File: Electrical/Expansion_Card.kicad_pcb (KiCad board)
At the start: 2 copper layers, 26 x 30 mm, 15 parts, among them J1 SJ-3501-SMT-TR, J2 SJ-3501-SMT-TR, P1 USB_C_Plug_USB2.0, U1 AP2112K-3.3, U2 PCM2906, U3 TPA6132A2RTE

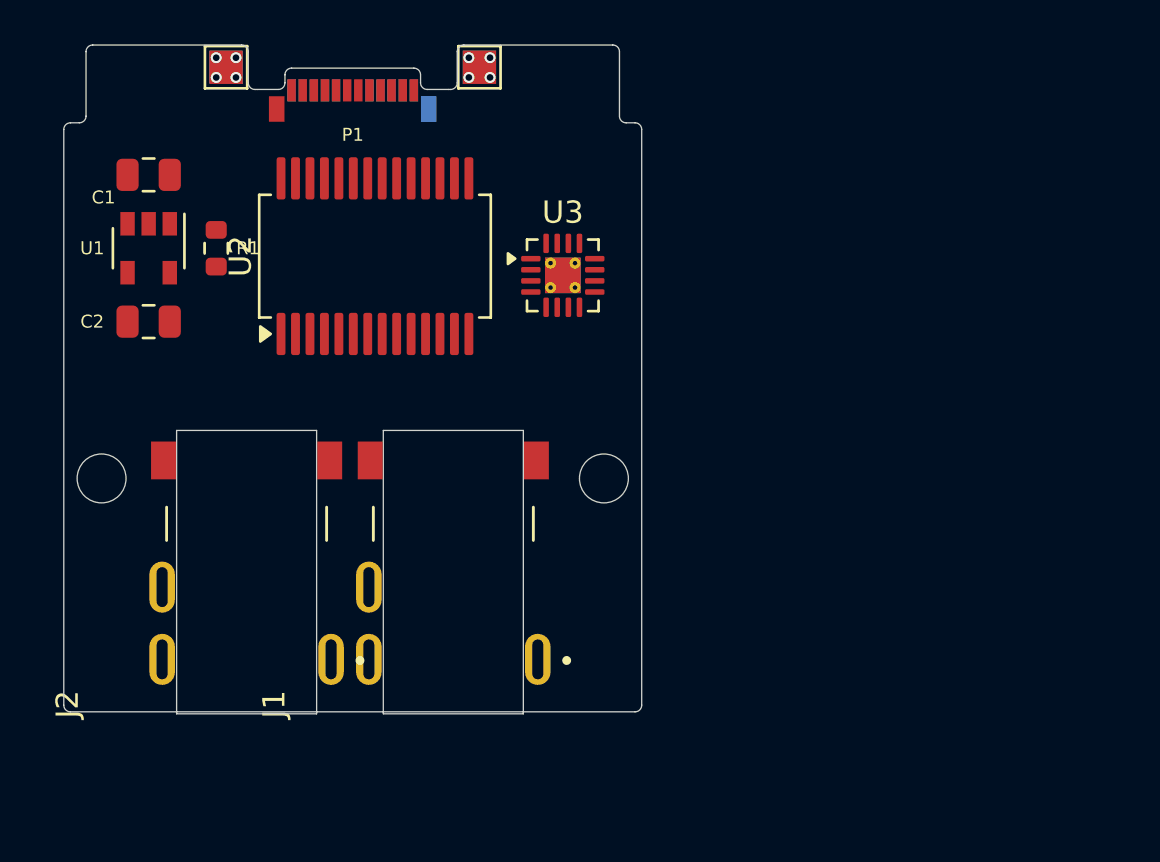
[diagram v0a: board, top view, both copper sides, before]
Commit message: New footprints and components added
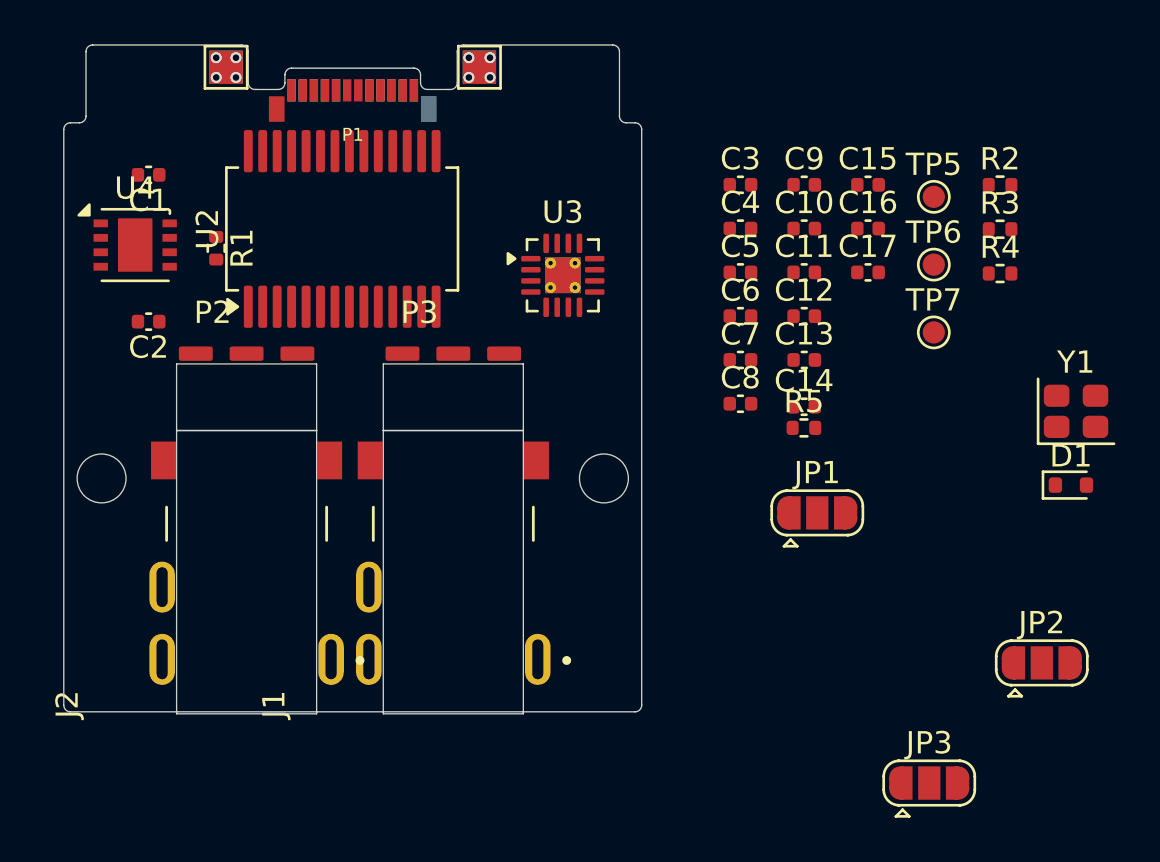
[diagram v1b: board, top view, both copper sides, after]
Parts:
- removed U1: AP2112K-3.3, Package_TO_SOT_SMD:SOT-23-5
- added C10: 1uF, Capacitor_SMD:C_0402_1005Metric, F.Cu at (160.3, 135.3)
- added C11: 1uF, Capacitor_SMD:C_0402_1005Metric, F.Cu at (160.3, 137.2)
- added C12: 1uF, Capacitor_SMD:C_0402_1005Metric, F.Cu at (160.3, 139.2)
- added C13: 1uF, Capacitor_SMD:C_0402_1005Metric, F.Cu at (160.3, 141.2)
- added C14: 1uF, Capacitor_SMD:C_0402_1005Metric, F.Cu at (160.3, 143.3)
- added C15: 1uF, Capacitor_SMD:C_0402_1005Metric, F.Cu at (163.2, 133.3)
- added C16: 2.2uF, Capacitor_SMD:C_0402_1005Metric, F.Cu at (163.2, 135.3)
- added C17: 2.2uF, Capacitor_SMD:C_0402_1005Metric, F.Cu at (163.2, 137.2)
- added C3: 8pF, Capacitor_SMD:C_0402_1005Metric, F.Cu at (157.4, 133.3)
- added C4: 8pF, Capacitor_SMD:C_0402_1005Metric, F.Cu at (157.4, 135.3)
- added C5: 10uF, Capacitor_SMD:C_0402_1005Metric, F.Cu at (157.4, 137.2)
- added C6: 10uF, Capacitor_SMD:C_0402_1005Metric, F.Cu at (157.4, 139.2)
- added C7: 1uF, Capacitor_SMD:C_0402_1005Metric, F.Cu at (157.4, 141.2)
- added C8: 1uF, Capacitor_SMD:C_0402_1005Metric, F.Cu at (157.4, 143.1)
- added C9: 1uF, Capacitor_SMD:C_0402_1005Metric, F.Cu at (160.3, 133.3)
- added D1: CDBU0130-HF, Diode_SMD:D_SOD-523, F.Cu at (172.3, 146.8)
- added JP1: SolderJumper_3_Open, Jumper:SolderJumper-3_P1.3mm_Open_RoundedPad1.0x1.5mm, F.Cu at (160.9, 148.1)
- added JP2: SolderJumper_3_Open, Jumper:SolderJumper-3_P1.3mm_Open_RoundedPad1.0x1.5mm, F.Cu at (171.0, 154.8)
- added JP3: SolderJumper_3_Open, Jumper:SolderJumper-3_P1.3mm_Open_RoundedPad1.0x1.5mm, F.Cu at (165.9, 160.2)
- added P2: ~, Expansion_Card:TX_RX_module, F.Cu at (135.2, 142.8)
- added P3: ~, Expansion_Card:TX_RX_module, F.Cu at (144.5, 142.8)
- added R2: 1.5k, Resistor_SMD:R_0402_1005Metric, F.Cu at (169.1, 133.3)
- added R3: 22, Resistor_SMD:R_0402_1005Metric, F.Cu at (169.1, 135.3)
- added R4: 22, Resistor_SMD:R_0402_1005Metric, F.Cu at (169.1, 137.3)
- added R5: 1M, Resistor_SMD:R_0402_1005Metric, F.Cu at (160.3, 144.2)
- added TP5: TestPoint, TestPoint:TestPoint_Pad_D1.0mm, F.Cu at (166.1, 133.8)
- added TP6: TestPoint, TestPoint:TestPoint_Pad_D1.0mm, F.Cu at (166.1, 136.9)
- added TP7: TestPoint, TestPoint:TestPoint_Pad_D1.0mm, F.Cu at (166.1, 139.9)
- added U4: LDLN050PUR, Package_DFN_QFN:DFN-8-1EP_3x3mm_P0.65mm_EP1.55x2.4mm, F.Cu at (130.2, 136.0)
- added Y1: 120-8-36B-CWY-TR, Crystal:Crystal_SMD_2520-4Pin_2.5x2.0mm, F.Cu at (172.5, 143.5)
- C1, C2: footprint Capacitor_SMD:C_0805_2012Metric -> Capacitor_SMD:C_0402_1005Metric
- R1: footprint Resistor_SMD:R_0603_1608Metric -> Resistor_SMD:R_0402_1005Metric
- moved U2 1.92 mm to (139.5, 135.3)
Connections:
- C2 pad 1: +3.3V -> VCC
- J1 pad 1: unconnected-(J1-Pad1) -> GND
- J1 pad 2: unconnected-(J1-Pad2) -> Net-(U3-OUTL)
- J1 pad 3: unconnected-(J1-Pad3) -> Net-(U3-OUTR)
- U2 pad 1: unconnected-(U2-D+-Pad1) -> Net-(U2-D+)
- U2 pad 10: unconnected-(U2-VCCCI-Pad10) -> VCCI
- U2 pad 11: unconnected-(U2-AGNDC-Pad11) -> GND
- U2 pad 14: unconnected-(U2-VCOM-Pad14) -> Net-(U2-VCOM)
- U2 pad 15: unconnected-(U2-VOUTR-Pad15) -> Net-(U2-VOUTR)
- U2 pad 16: unconnected-(U2-VOUTL-Pad16) -> Net-(U2-VOUTL)
- U2 pad 17: unconnected-(U2-VCCP1I-Pad17) -> Net-(U2-VCCP1I)
- U2 pad 18: unconnected-(U2-AGNDP-Pad18) -> GND
- U2 pad 19: unconnected-(U2-VCCP2I-Pad19) -> Net-(U2-VCCP2I)
- U2 pad 2: unconnected-(U2-D--Pad2) -> Net-(U2-D-)
- U2 pad 20: unconnected-(U2-XTO-Pad20) -> Net-(U2-XTO)
- U2 pad 21: unconnected-(U2-XTI-Pad21) -> Net-(U2-XTI)
- U2 pad 22: unconnected-(U2-AGNDX-Pad22) -> GND
- U2 pad 23: unconnected-(U2-VCCXI-Pad23) -> Net-(U2-VCCXI)
- U2 pad 26: unconnected-(U2-DGND-Pad26) -> GND
- U2 pad 27: unconnected-(U2-VDDI-Pad27) -> VDDI
- U2 pad 28: unconnected-(U2-~{SSPND}-Pad28) -> /EN
- U2 pad 3: unconnected-(U2-VBUS-Pad3) -> VBUS
- U2 pad 4: unconnected-(U2-DGNDU-Pad4) -> GND
- U2 pad 5: unconnected-(U2-HID0-Pad5) -> Net-(U2-HID0)
- U2 pad 6: unconnected-(U2-HID1-Pad6) -> Net-(U2-HID1)
- U2 pad 7: unconnected-(U2-HID2-Pad7) -> Net-(U2-HID2)
- U2 pad 8: unconnected-(U2-SEL0-Pad8) -> VDDI
- U2 pad 9: unconnected-(U2-SEL1-Pad9) -> VDDI
- U3 pad 1: unconnected-(U3-INL--Pad1) -> Net-(U3-INL-)
- U3 pad 10: unconnected-(U3-PGND-Pad10) -> GND
- U3 pad 11: unconnected-(U3-CPP-Pad11) -> Net-(U3-CPP)
- U3 pad 12: unconnected-(U3-HPVDD-Pad12) -> Net-(U3-HPVDD)
- U3 pad 13: unconnected-(U3-EN-Pad13) -> /EN
- U3 pad 14: unconnected-(U3-VDD-Pad14) -> Net-(JP3-C)
- U3 pad 15: unconnected-(U3-SGND-Pad15) -> GND
- U3 pad 16: unconnected-(U3-OUTL-Pad16) -> Net-(U3-OUTL)
- U3 pad 17: unconnected-(U3-EP-Pad17) -> GND
- U3 pad 2: unconnected-(U3-INL+-Pad2) -> GND
- U3 pad 3: unconnected-(U3-INR+-Pad3) -> GND
- U3 pad 4: unconnected-(U3-INR--Pad4) -> Net-(U3-INR-)
- U3 pad 5: unconnected-(U3-OUTR-Pad5) -> Net-(U3-OUTR)
- U3 pad 6: unconnected-(U3-G0-Pad6) -> /G0
- U3 pad 7: unconnected-(U3-G1-Pad7) -> /G1
- U3 pad 8: unconnected-(U3-HPVSS-Pad8) -> Net-(U3-HPVSS)
- U3 pad 9: unconnected-(U3-CPN-Pad9) -> Net-(U3-CPN)

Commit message: Schematic completed + basic layout
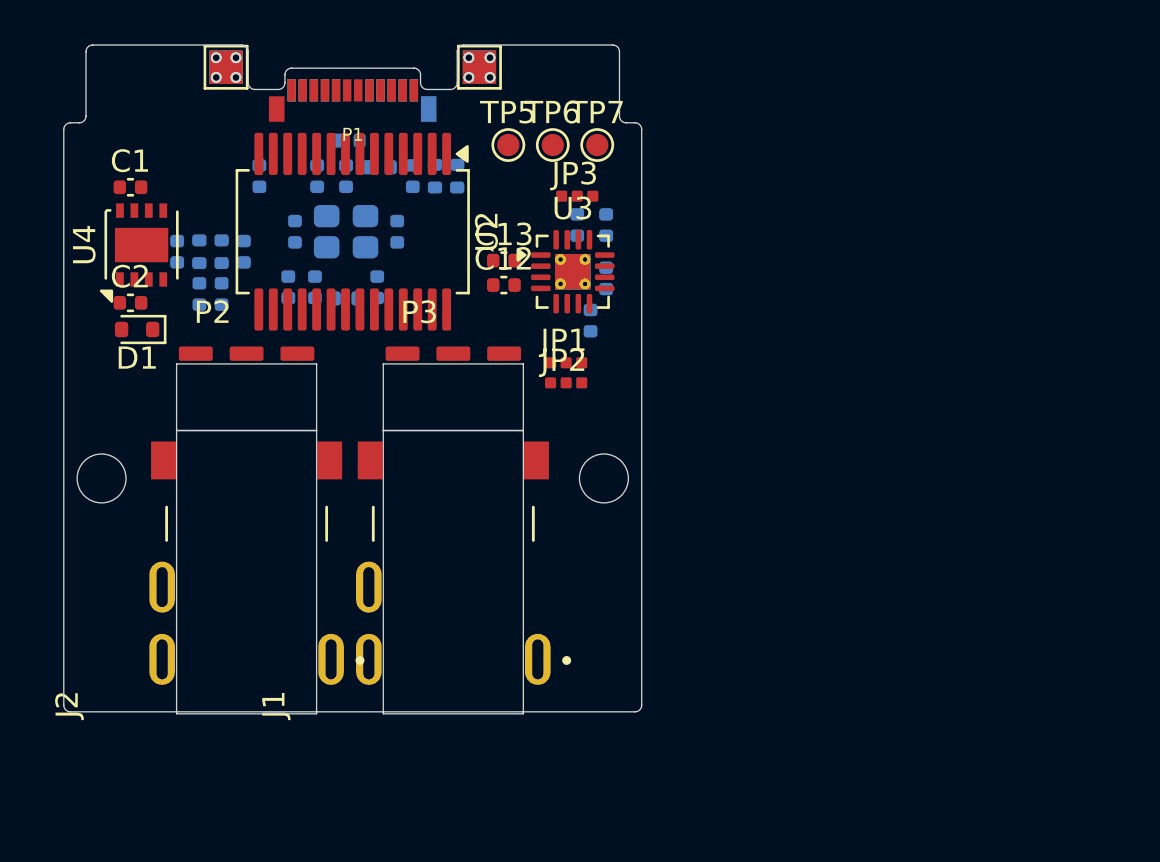
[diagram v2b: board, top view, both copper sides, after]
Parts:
- added C18: 1uF, Capacitor_SMD:C_0402_1005Metric, B.Cu at (134.1, 138.2)
- added C19: 1uF, Capacitor_SMD:C_0402_1005Metric, B.Cu at (133.1, 138.2)
- added C20: 1nF, Capacitor_SMD:C_0402_1005Metric, B.Cu at (132.1, 136.3)
- added C21: 1nF, Capacitor_SMD:C_0402_1005Metric, B.Cu at (135.1, 136.3)
- added R7: 1k, Resistor_SMD:R_0402_1005Metric, B.Cu at (133.1, 136.3)
- added R8: 1k, Resistor_SMD:R_0402_1005Metric, B.Cu at (134.1, 136.3)
- C10, C11, C14, C15, C16, C17, C3, C4, C5, C6, C7, C8, C9, R1, R2, R3, R4, R5, Y1: moved to B.Cu
- JP1, JP2, JP3: footprint Jumper:SolderJumper-3_P1.3mm_Open_RoundedPad1.0x1.5mm -> Expansion_Card:Jumper_small_straight
- moved D1 42.6 mm to (130.3, 139.8), turned to 180 degrees
- moved Y1 33.8 mm to (139.7, 135.4)
- moved JP3 30.8 mm to (150.1, 133.8)
- moved R2 27.9 mm to (141.2, 132.5)
- moved R4 25.8 mm to (143.7, 132.9), turned to -90 degrees
- moved JP2 24.8 mm to (149.6, 142.2)
- moved R3 24.5 mm to (144.7, 132.9), turned to -90 degrees
- moved C6 22.5 mm to (135.8, 132.9), turned to -90 degrees
- moved R5 21.4 mm to (139.7, 138.4), turned to 180 degrees
- moved C10 20.7 mm to (139.7, 132.9), turned to 90 degrees
- moved C7 20.6 mm to (137.1, 137.9), turned to 90 degrees
- moved C3 20.2 mm to (137.4, 135.4), turned to -90 degrees
- moved C8 19.8 mm to (138.3, 137.9), turned to 90 degrees
- moved C9 19.8 mm to (141.1, 137.9), turned to 90 degrees
- moved C5 19.5 mm to (138.4, 132.9), turned to -90 degrees
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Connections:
- J1 pad 4: unconnected-(J1-Pad4) -> Net-(U3-OUTL)
- J1 pad 5: unconnected-(J1-Pad5) -> GND
- J2 pad 1: unconnected-(J2-Pad1) -> GND
- J2 pad 2: unconnected-(J2-Pad2) -> Net-(C18-Pad1)
- J2 pad 3: unconnected-(J2-Pad3) -> Net-(C19-Pad1)
- J2 pad 4: unconnected-(J2-Pad4) -> Net-(C18-Pad1)
- J2 pad 5: unconnected-(J2-Pad5) -> GND
- P2 pad 1: unconnected-(P2-OUT-Pad1) -> Net-(P2-OUT)
- P2 pad 2: unconnected-(P2-GND-Pad2) -> GND
- P2 pad 3: unconnected-(P2-VCC-Pad3) -> VCC
- P3 pad 1: unconnected-(P3-GND-Pad1) -> GND
- P3 pad 2: unconnected-(P3-VCC-Pad2) -> VCC
- P3 pad 3: unconnected-(P3-IN-Pad3) -> Net-(P3-IN)
- U2 pad 12: unconnected-(U2-VINL-Pad12) -> Net-(U2-VINL)
- U2 pad 13: unconnected-(U2-VINR-Pad13) -> Net-(U2-VINR)
- U2 pad 24: unconnected-(U2-DIN-Pad24) -> Net-(P2-OUT)
- U2 pad 25: unconnected-(U2-DOUT-Pad25) -> Net-(P3-IN)

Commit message: Routing + output
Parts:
- removed TP1, TP2, TP3, TP4: TestPoint, TestPoint:TestPoint_Pad_1.5x1.5mm
- added P4: ~, Expansion_Card:TX_RX_module, B.Cu at (144.5, 142.8)
- added P5: ~, Expansion_Card:TX_RX_module, B.Cu at (135.2, 142.8)
- added R6: 150k, Resistor_SMD:R_0402_1005Metric, B.Cu at (130.0, 136.6)
- added R9: 300k, Resistor_SMD:R_0402_1005Metric, B.Cu at (130.0, 137.6)
- JP1, JP2: moved to B.Cu
- moved TP7 3.08 mm to (148.5, 129.7)
- moved C17 1.89 mm to (148.6, 133.9), turned to 180 degrees
- moved C18 1.55 mm to (133.7, 136.7)
- moved C19 1.55 mm to (132.7, 136.7)
- moved C20 1.55 mm to (131.7, 134.8)
- moved C21 1.55 mm to (134.7, 134.8)
- moved R7 1.55 mm to (132.7, 134.8)
- moved R8 1.55 mm to (133.7, 134.8)
- moved C13 1.39 mm to (146.1, 135.5), turned to -90 degrees
- moved C14 1.17 mm to (149.7, 138.8)
- moved C15 1.17 mm to (150.4, 136.9)
- moved C16 1.17 mm to (150.4, 134.5)
- moved U3 1.17 mm to (148.9, 136.6)
- moved R1 1.16 mm to (138.7, 131.0), turned to 180 degrees
- moved R3 1.00 mm to (144.7, 133.9), turned to 90 degrees
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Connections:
- J1 pad 2: Net-(U3-OUTL) -> unconnected-(J1-Pad2)
- J2 pad 2: Net-(C18-Pad1) -> unconnected-(J2-Pad2)
- U4 pad 3: unconnected-(U4-FB-Pad3) -> Net-(U4-FB)
- Y1 pad 2: Net-(Y1-G-Pad2) -> GND
- Y1 pad 4: Net-(Y1-G-Pad2) -> GND
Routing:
- net /EN: track 0.00 -> 26.7 mm, vias 0 -> 3
- net GND: track 0.00 -> 26.1 mm, vias 8 -> 116
- net Net-(U3-OUTR): track 0.00 -> 19.4 mm, vias 0 -> 1
- net Net-(P2-OUT): track 0.00 -> 17.2 mm, vias 0 -> 1
- net VCCI: track 0.00 -> 15.6 mm, vias 0 -> 2
- net Net-(U2-VOUTL): track 0.00 -> 15.1 mm, vias 0 -> 2
- net Net-(C19-Pad1): track 0.00 -> 14.7 mm, vias 0 -> 1
- net Net-(U3-OUTL): track 0.00 -> 13.0 mm, vias 0 -> 2
- net Net-(U2-VOUTR): track 0.00 -> 12.5 mm, vias 0 -> 2
- net Net-(C18-Pad1): track 0.00 -> 12.2 mm, vias 0 -> 2
- net VDDI: track 0.00 -> 10.8 mm, vias 0 -> 2
- net Net-(U2-HID2): track 0.00 -> 9.45 mm, vias 0 -> 2
- net /USB_DP: track 0.00 -> 9.41 mm, vias 0 -> 2
- net Net-(U2-D+): track 0.00 -> 8.79 mm, vias 0 -> 1
- net Net-(U2-HID1): track 0.00 -> 8.14 mm, vias 0 -> 2
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- added copper zone on B.Cu, net GND
- added copper zone on F.Cu, net GND
- added copper zone on In1.Cu, net GND
- added copper zone on In3.Cu, net GND
- added copper zone on F.Cu, net VBUS
- added copper zone on In4.Cu, net VBUS
- added copper zone on F.Cu, net VCC
- added copper zone on In4.Cu, net VCC
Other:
- outline, holes or cut-outs redrawn
- copper layers 2 -> 6
- board text added: "G0"
- board text added: "G1"
- board text added: "RX"
- board text added: "TX"
